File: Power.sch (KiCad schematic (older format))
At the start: 15 parts, among them U301 AOZ6605PI-1

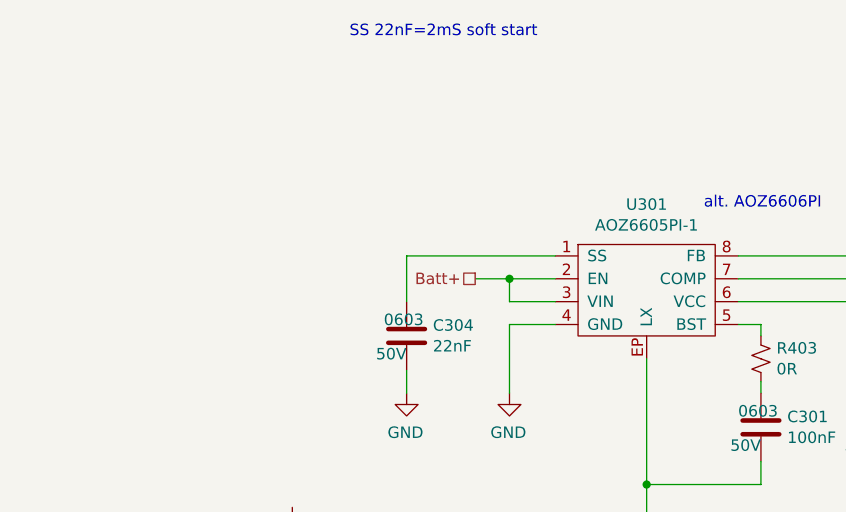
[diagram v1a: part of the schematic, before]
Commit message: Placeholders for some connectors.
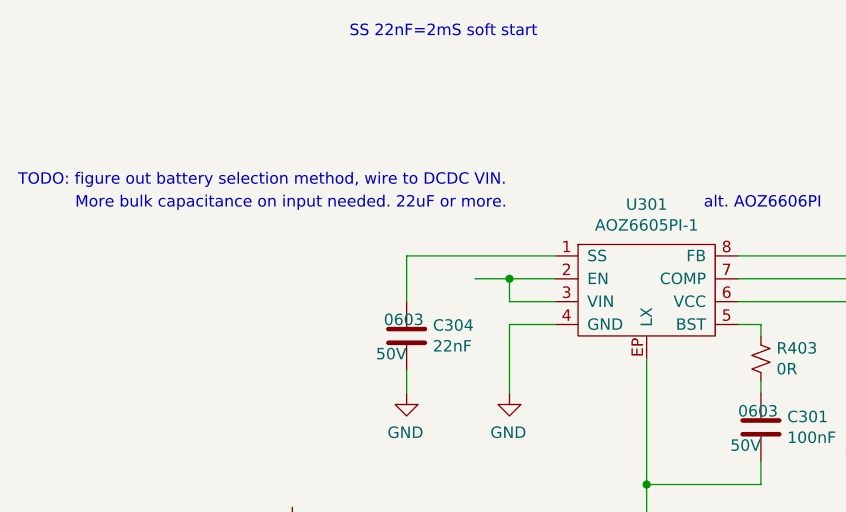
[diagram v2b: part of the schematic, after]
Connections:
- net Batt+: no longer names the net of U301.2 (EN), U301.3 (VIN)
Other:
- note added: "More bulk capacitance on input needed. 22uF or more."
- note added: "TODO: figure out battery selection method, wire to DCDC VIN."
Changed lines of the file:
@@
 EESchema Schematic File Version 4
 LIBS:dingo-hat-cache
-EELAYER 29 0
+EELAYER 30 0
 EELAYER END
 $Descr A4 11693 8268
@@
 	1    0    0    -1
 $EndComp
-Text HLabel 4000 2950 0    50   UnSpc ~ 0
-Batt+
 Wire Wire Line
 	4000 2950 4150 2950
 Connection ~ 4150 2950
+Text Notes 2250 2650 0    50   ~ 0
+More bulk capacitance on input needed. 22uF or more.
+Text Notes 2000 2550 0    50   ~ 0
+TODO: figure out battery selection method, wire to DCDC VIN.
 $EndSCHEMATC

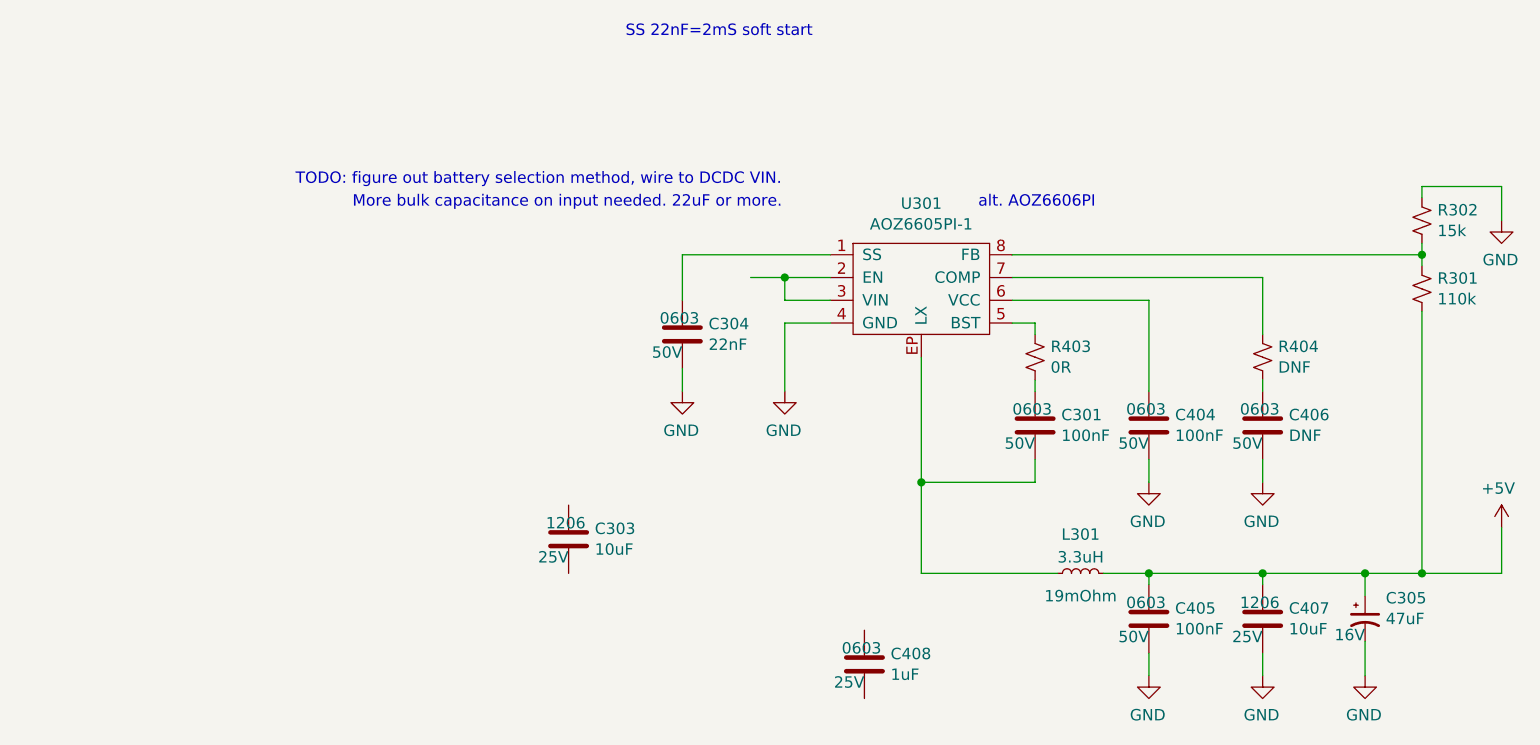
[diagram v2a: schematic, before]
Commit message: Cleaning up some nets, adding input caps on power.
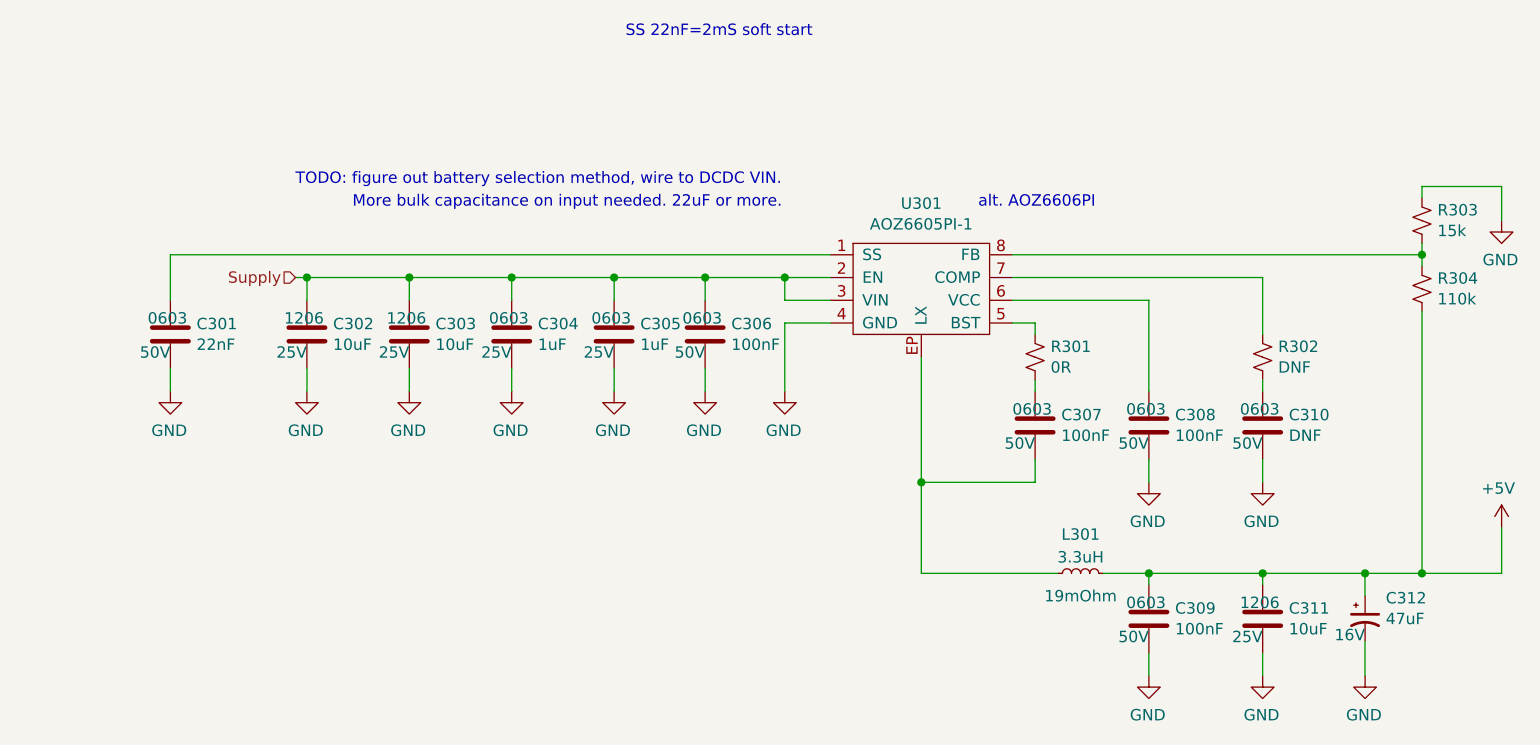
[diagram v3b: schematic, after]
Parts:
- added C302: 10uF, Capacitors_SMD:C_1206, symbol Device:C
- added C305: 1uF, Capacitors_SMD:C_0603, symbol Device:C
- added C306: 100nF, Capacitors_SMD:C_0603, symbol Device:C
- renumbered C304 to C301, C408 to C304, C301 to C307, C404 to C308, C405 to C309, C406 to C310, C407 to C311, C305 to C312, R403 to R301, R404 to R302, R302 to R303, R301 to R304
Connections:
- net GND: now also C303.2, C304.2, C302.2, C305.2, C306.2
- net Supply: now reaches U301.2 (EN), U301.3 (VIN)
- net Supply: now also C303.1, C304.1, C302.1, C305.1, C306.1
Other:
- moved on the sheet: C301, C303, C304

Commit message: Power protection.
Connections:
- net Supply renamed BatterySupply
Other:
- note removed: "More bulk capacitance on input needed. 22uF or more."
- moved on the sheet: C301
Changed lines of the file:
@@
 L Device:C C?
 U 1 1 5DBE04EC
-P 1450 3200
+P 950 3200
 AR Path="/5DBE04EC" Ref="C?"  Part="1"
 AR Path="/5DA95EB0/5DBE04EC" Ref="C301"  Part="1"
-F 0 "C301" H 1565 3246 50  0000 L CNN
-F 1 "22nF" H 1565 3155 50  0000 L CNN
-F 2 "Capacitors_SMD:C_0603" H 1488 3050 50  0001 C CNN
-F 3 "~" H 1450 3200 50  0001 C CNN
-F 4 "0603" H 1350 3300 50  0000 L TNN "Package"
-F 5 "CAP CER 0.022UF 50V X7R 0603" H 1450 3200 50  0001 C CNN "Description"
-F 6 "50V" H 1450 3150 50  0000 R TNN "Voltage Rating"
-F 7 "https://www.digikey.com.au/product-detail/en/kemet/C0603C223K5RACTU/399-1280-1-ND/416056" H 1450 3200 50  0001 C CNN "Link"
-F 8 "Digi-Key" H 1450 3200 50  0001 C CNN "Supplier 1"
-F 9 "399-1280-1-ND" H 1450 3200 50  0001 C CNN "Supplier Part Number 1"
-F 10 "0.15000" H 1450 3200 50  0001 C CNN "Unit Cost A$"
-	1    1450 3200
+F 0 "C301" H 1065 3246 50  0000 L CNN
+F 1 "22nF" H 1065 3155 50  0000 L CNN
+F 2 "Capacitors_SMD:C_0603" H 988 3050 50  0001 C CNN
+F 3 "~" H 950 3200 50  0001 C CNN
+F 4 "0603" H 850 3300 50  0000 L TNN "Package"
+F 5 "CAP CER 0.022UF 50V X7R 0603" H 950 3200 50  0001 C CNN "Description"
+F 6 "50V" H 950 3150 50  0000 R TNN "Voltage Rating"
+F 7 "https://www.digikey.com.au/product-detail/en/kemet/C0603C223K5RACTU/399-1280-1-ND/416056" H 950 3200 50  0001 C CNN "Link"
+F 8 "Digi-Key" H 950 3200 50  0001 C CNN "Supplier 1"
+F 9 "399-1280-1-ND" H 950 3200 50  0001 C CNN "Supplier Part Number 1"
+F 10 "0.15000" H 950 3200 50  0001 C CNN "Unit Cost A$"
+	1    950  3200
 	1    0    0    -1
 $EndComp
@@
 L power:GND #PWR?
 U 1 1 5DC01D58
-P 1450 3450
+P 950 3450
 AR Path="/5DC01D58" Ref="#PWR?"  Part="1"
 AR Path="/5DA95EB0/5DC01D58" Ref="#PWR0301"  Part="1"
-F 0 "#PWR0301" H 1450 3200 50  0001 C CNN
-F 1 "GND" H 1455 3277 50  0000 C CNN
-F 2 "" H 1450 3450 50  0001 C CNN
-F 3 "" H 1450 3450 50  0001 C CNN
-	1    1450 3450
-	-1   0    0    -1
-$EndComp
-Wire Wire Line
-	1450 3350 1450 3450
-Wire Wire Line
-	1450 3050 1450 2850
+F 0 "#PWR0301" H 950 3200 50  0001 C CNN
+F 1 "GND" H 955 3277 50  0000 C CNN
+F 2 "" H 950 3450 50  0001 C CNN
+F 3 "" H 950 3450 50  0001 C CNN
+	1    950  3450
+	-1   0    0    -1
+$EndComp
+Wire Wire Line
+	950  3350 950  3450
+Wire Wire Line
+	950  3050 950  2850
 Text Notes 3450 1900 0    50   ~ 0
 SS 22nF=2mS soft start
@@
 	1    0    0    -1
 $EndComp
-Text Notes 2250 2650 0    50   ~ 0
-More bulk capacitance on input needed. 22uF or more.
 Text Notes 2000 2550 0    50   ~ 0
 TODO: figure out battery selection method, wire to DCDC VIN.
-Text HLabel 2000 2950 0    50   Input ~ 0
-Supply
-Wire Wire Line
-	2000 2950 2050 2950
+Text HLabel 1750 2950 0    50   Input ~ 0
+BatterySupply
 $Comp
 L power:GND #PWR?
@@
 	3800 3350 3800 3450
 Wire Wire Line
-	1450 2850 4350 2850
+	950  2850 4350 2850
+Wire Wire Line
+	1750 2950 2050 2950
 $EndSCHEMATC

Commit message: Filling in some footprints, cleaning up schematic.
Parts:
- L301: footprint (none) -> libs:Inductor-SMT-MPLCH0740
- U301: footprint (none) -> libs:SOIC-8-EP--AOZ6605PI-1
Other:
- note removed: "TODO: figure out battery selection method, wire to DCDC VIN."
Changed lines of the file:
@@
 F 0 "U301" H 4750 3375 50  0000 C CNN
 F 1 "AOZ6605PI-1" H 4750 3284 50  0000 C CNN
-F 2 "" H 4850 3000 50  0001 C CNN
+F 2 "libs:SOIC-8-EP--AOZ6605PI-1" H 4850 3000 50  0001 C CNN
 F 3 "http://www.aosmd.com/res/data_sheets/AOZ6605PI-1.pdf" H 4850 3000 50  0001 C CNN
 F 4 "https://www.digikey.com.au/product-detail/en/alpha-omega-semiconductor-inc/AOZ6605PI-1/785-1853-1-ND/10258148" H 4750 3000 50  0001 C CNN "Link"
@@
 F 0 "L301" V 5650 4250 50  0000 C BNN
 F 1 "3.3uH" V 5550 4250 50  0000 C BNN
-F 2 "" H 5450 4250 50  0001 C CNN
+F 2 "libs:Inductor-SMT-MPLCH0740" H 5450 4250 50  0001 C CNN
 F 3 "~" H 5450 4250 50  0001 C CNN
 F 4 "FIXED IND 3.3UH 7.8A 19 MOHM SMD" V 5543 4250 50  0001 C CNN "Description"
@@
 Wire Wire Line
 	950  3050 950  2850
-Text Notes 3450 1900 0    50   ~ 0
+Text Notes 850  2800 0    50   ~ 0
 SS 22nF=2mS soft start
 $Comp
@@
 	1    0    0    -1
 $EndComp
-Text Notes 2000 2550 0    50   ~ 0
-TODO: figure out battery selection method, wire to DCDC VIN.
 Text HLabel 1750 2950 0    50   Input ~ 0
 BatterySupply

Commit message: Pushing and shoving components.
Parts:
- removed C304: 1uF, Capacitors_SMD:C_0603, symbol Device:C
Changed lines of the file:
@@
 	7300 4050 7300 4250
 Connection ~ 6950 4250
-$Comp
-L Device:C C?
-U 1 1 5DEA1AB8
-P 2950 3200
-AR Path="/5DEA1AB8" Ref="C?"  Part="1"
-AR Path="/5DA95EB0/5DEA1AB8" Ref="C304"  Part="1"
-F 0 "C304" H 3065 3246 50  0000 L CNN
-F 1 "1uF" H 3065 3155 50  0000 L CNN
-F 2 "Capacitors_SMD:C_0603" H 2988 3050 50  0001 C CNN
-F 3 "~" H 2950 3200 50  0001 C CNN
-F 4 "0603" H 2850 3300 50  0000 L TNN "Package"
-F 5 "CAP CER 1UF 25V X5R 0603" H 2950 3200 50  0001 C CNN "Description"
-F 6 "25V" H 2950 3150 50  0000 R TNN "Voltage Rating"
-F 7 "https://www.digikey.com.au/product-detail/en/yageo/CC0603KRX5R8BB105/311-1445-1-ND/2833751" H 2950 3200 50  0001 C CNN "Link"
-F 8 "Digi-Key" H 2950 3200 50  0001 C CNN "Supplier 1"
-F 9 "311-1445-1-ND" H 2950 3200 50  0001 C CNN "Supplier Part Number 1"
-F 10 "0.15000" H 2950 3200 50  0001 C CNN "Unit Cost A$"
-	1    2950 3200
-	1    0    0    -1
-$EndComp
 Text HLabel 1750 2950 0    50   Input ~ 0
 BatterySupply
@@
 	2050 2950 2500 2950
 Connection ~ 2500 2950
-Wire Wire Line
-	2500 2950 2950 2950
-$Comp
-L power:GND #PWR?
-U 1 1 5DC20C47
-P 2950 3450
-AR Path="/5DC20C47" Ref="#PWR?"  Part="1"
-AR Path="/5DA95EB0/5DC20C47" Ref="#PWR0304"  Part="1"
-F 0 "#PWR0304" H 2950 3200 50  0001 C CNN
-F 1 "GND" H 2955 3277 50  0000 C CNN
-F 2 "" H 2950 3450 50  0001 C CNN
-F 3 "" H 2950 3450 50  0001 C CNN
-	1    2950 3450
-	-1   0    0    -1
-$EndComp
-Wire Wire Line
-	2950 3350 2950 3450
-Wire Wire Line
-	2950 3050 2950 2950
-Connection ~ 2950 2950
-Wire Wire Line
-	2950 2950 3400 2950
 $Comp
 L Device:C C?
@@
 Wire Wire Line
 	1750 2950 2050 2950
+Wire Wire Line
+	2500 2950 3400 2950
 $EndSCHEMATC

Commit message: Power net fill routing.
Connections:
- net LX: now reaches C307.2, L301.1, U301.EP (LX)
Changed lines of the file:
@@
 $Descr A4 11693 8268
 encoding utf-8
-Sheet 2 3
+Sheet 3 3
 Title ""
 Date ""
@@
 Wire Wire Line
 	2500 2950 3400 2950
+Text Label 4750 3850 0    50   ~ 0
+LX
 $EndSCHEMATC

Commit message: updated footprints to handsolder
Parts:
- C301, C305, C306, C307, C308, C309, C310: footprint Capacitors_SMD:C_0603 -> Capacitor_SMD:C_0603_1608Metric_Pad1.05x0.95mm_HandSolder
- C302, C303, C311: footprint Capacitors_SMD:C_1206 -> Capacitor_SMD:C_1206_3216Metric_Pad1.42x1.75mm_HandSolder
- R301, R302, R303, R304: footprint Resistors_SMD:R_0603 -> Resistor_SMD:R_0603_1608Metric_Pad1.05x0.95mm_HandSolder
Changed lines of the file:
@@
 F 0 "R304" H 7018 3046 50  0000 L CNN
 F 1 "110k" H 7018 2955 50  0000 L CNN
-F 2 "Resistors_SMD:R_0603" H 6950 3000 50  0001 C CNN
+F 2 "Resistor_SMD:R_0603_1608Metric_Pad1.05x0.95mm_HandSolder" H 6950 3000 50  0001 C CNN
 F 3 "~" H 6950 3000 50  0001 C CNN
 	1    6950 3000
@@
 F 0 "R303" H 7018 2746 50  0000 L CNN
 F 1 "15k" H 7018 2655 50  0000 L CNN
-F 2 "Resistors_SMD:R_0603" H 6950 2700 50  0001 C CNN
+F 2 "Resistor_SMD:R_0603_1608Metric_Pad1.05x0.95mm_HandSolder" H 6950 2700 50  0001 C CNN
 F 3 "~" H 6950 2700 50  0001 C CNN
 	1    6950 2700
@@
 F 0 "C301" H 1065 3246 50  0000 L CNN
 F 1 "22nF" H 1065 3155 50  0000 L CNN
-F 2 "Capacitors_SMD:C_0603" H 988 3050 50  0001 C CNN
+F 2 "Capacitor_SMD:C_0603_1608Metric_Pad1.05x0.95mm_HandSolder" H 988 3050 50  0001 C CNN
 F 3 "~" H 950 3200 50  0001 C CNN
 F 4 "0603" H 850 3300 50  0000 L TNN "Package"
@@
 F 0 "C303" H 2615 3246 50  0000 L CNN
 F 1 "10uF" H 2615 3155 50  0000 L CNN
-F 2 "Capacitors_SMD:C_1206" H 2538 3050 50  0001 C CNN
+F 2 "Capacitor_SMD:C_1206_3216Metric_Pad1.42x1.75mm_HandSolder" H 2538 3050 50  0001 C CNN
 F 3 "~" H 2500 3200 50  0001 C CNN
 F 4 "1206" H 2400 3300 50  0000 L TNN "Package"
@@
 F 0 "C307" H 5365 3646 50  0000 L CNN
 F 1 "100nF" H 5365 3555 50  0000 L CNN
-F 2 "Capacitors_SMD:C_0603" H 5288 3450 50  0001 C CNN
+F 2 "Capacitor_SMD:C_0603_1608Metric_Pad1.05x0.95mm_HandSolder" H 5288 3450 50  0001 C CNN
 F 3 "~" H 5250 3600 50  0001 C CNN
 F 4 "0603" H 5150 3700 50  0000 L TNN "Package"
@@
 F 0 "R301" H 5182 3254 50  0000 R CNN
 F 1 "0R" H 5182 3345 50  0000 R CNN
-F 2 "Resistors_SMD:R_0603" H 5250 3300 50  0001 C CNN
+F 2 "Resistor_SMD:R_0603_1608Metric_Pad1.05x0.95mm_HandSolder" H 5250 3300 50  0001 C CNN
 F 3 "~" H 5250 3300 50  0001 C CNN
 	1    5250 3300
@@
 F 0 "C308" H 5865 3646 50  0000 L CNN
 F 1 "100nF" H 5865 3555 50  0000 L CNN
-F 2 "Capacitors_SMD:C_0603" H 5788 3450 50  0001 C CNN
+F 2 "Capacitor_SMD:C_0603_1608Metric_Pad1.05x0.95mm_HandSolder" H 5788 3450 50  0001 C CNN
 F 3 "~" H 5750 3600 50  0001 C CNN
 F 4 "0603" H 5650 3700 50  0000 L TNN "Package"
@@
 F 0 "R302" H 6182 3254 50  0000 R CNN
 F 1 "DNF" H 6182 3345 50  0000 R CNN
-F 2 "Resistors_SMD:R_0603" H 6250 3300 50  0001 C CNN
+F 2 "Resistor_SMD:R_0603_1608Metric_Pad1.05x0.95mm_HandSolder" H 6250 3300 50  0001 C CNN
 F 3 "~" H 6250 3300 50  0001 C CNN
 	1    6250 3300
@@
 F 0 "C310" H 6365 3646 50  0000 L CNN
 F 1 "DNF" H 6365 3555 50  0000 L CNN
-F 2 "Capacitors_SMD:C_0603" H 6288 3450 50  0001 C CNN
+F 2 "Capacitor_SMD:C_0603_1608Metric_Pad1.05x0.95mm_HandSolder" H 6288 3450 50  0001 C CNN
 F 3 "~" H 6250 3600 50  0001 C CNN
 F 4 "0603" H 6150 3700 50  0000 L TNN "Package"
@@
 F 0 "C309" H 5865 4496 50  0000 L CNN
 F 1 "100nF" H 5865 4405 50  0000 L CNN
-F 2 "Capacitors_SMD:C_0603" H 5788 4300 50  0001 C CNN
+F 2 "Capacitor_SMD:C_0603_1608Metric_Pad1.05x0.95mm_HandSolder" H 5788 4300 50  0001 C CNN
 F 3 "~" H 5750 4450 50  0001 C CNN
 F 4 "0603" H 5650 4550 50  0000 L TNN "Package"
@@
 F 0 "C311" H 6365 4496 50  0000 L CNN
 F 1 "10uF" H 6365 4405 50  0000 L CNN
-F 2 "Capacitors_SMD:C_1206" H 6288 4300 50  0001 C CNN
+F 2 "Capacitor_SMD:C_1206_3216Metric_Pad1.42x1.75mm_HandSolder" H 6288 4300 50  0001 C CNN
 F 3 "~" H 6250 4450 50  0001 C CNN
 F 4 "1206" H 6150 4550 50  0000 L TNN "Package"
@@
 F 0 "C302" H 2165 3246 50  0000 L CNN
 F 1 "10uF" H 2165 3155 50  0000 L CNN
-F 2 "Capacitors_SMD:C_1206" H 2088 3050 50  0001 C CNN
+F 2 "Capacitor_SMD:C_1206_3216Metric_Pad1.42x1.75mm_HandSolder" H 2088 3050 50  0001 C CNN
 F 3 "~" H 2050 3200 50  0001 C CNN
 F 4 "1206" H 1950 3300 50  0000 L TNN "Package"
@@
 F 0 "C305" H 3515 3246 50  0000 L CNN
 F 1 "1uF" H 3515 3155 50  0000 L CNN
-F 2 "Capacitors_SMD:C_0603" H 3438 3050 50  0001 C CNN
+F 2 "Capacitor_SMD:C_0603_1608Metric_Pad1.05x0.95mm_HandSolder" H 3438 3050 50  0001 C CNN
 F 3 "~" H 3400 3200 50  0001 C CNN
 F 4 "0603" H 3300 3300 50  0000 L TNN "Package"
@@
 F 0 "C306" H 3915 3246 50  0000 L CNN
 F 1 "100nF" H 3915 3155 50  0000 L CNN
-F 2 "Capacitors_SMD:C_0603" H 3838 3050 50  0001 C CNN
+F 2 "Capacitor_SMD:C_0603_1608Metric_Pad1.05x0.95mm_HandSolder" H 3838 3050 50  0001 C CNN
 F 3 "~" H 3800 3200 50  0001 C CNN
 F 4 "0603" H 3700 3300 50  0000 L TNN "Package"
